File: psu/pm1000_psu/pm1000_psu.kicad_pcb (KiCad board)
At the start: 2 copper layers, 101.5 x 32 mm, 35 parts, among them J1 44V A, J2 44V B, J3 Screw_Terminal_01x04, J4 48V phantom, U1 LM317_TO-220, U2 LM317_TO-220, U3 LM317_TO-220

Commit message: rework the psu layout a bit
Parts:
- added C11: 100n, Capacitor_THT:C_Disc_D5.0mm_W2.5mm_P2.50mm, F.Cu at (96.0, 62.5)
- added C5: 100n, Capacitor_THT:C_Disc_D5.0mm_W2.5mm_P2.50mm, F.Cu at (52.2, 76.0)
- added C9: 100n, Capacitor_THT:C_Disc_D5.0mm_W2.5mm_P2.50mm, F.Cu at (115.8, 44.0)
- added D10: LED_Small, LED_THT:LED_D3.0mm, F.Cu at (88.0, 63.8)
- added D8: LED_Small, LED_THT:LED_D3.0mm, F.Cu at (116.5, 60.7)
- added D9: LED_Small, LED_THT:LED_D3.0mm, F.Cu at (47.0, 74.8)
- added J2: , Connector_Molex:Molex_KK-254_AE-6410-02A_1x02_P2.54mm_Vertical, F.Cu at (121.5, 54.7)
- added R12: 2k2, Resistor_THT:R_Axial_DIN0207_L6.3mm_D2.5mm_P10.16mm_Horizontal, F.Cu at (101.9, 57.0)
- added R13: 2k2, Resistor_THT:R_Axial_DIN0207_L6.3mm_D2.5mm_P10.16mm_Horizontal, F.Cu at (45.5, 56.6)
- added R14: 2k2, Resistor_THT:R_Axial_DIN0207_L6.3mm_D2.5mm_P10.16mm_Horizontal, F.Cu at (86.4, 58.5)
- added R3: 2k2, Resistor_THT:R_Axial_DIN0207_L6.3mm_D2.5mm_P10.16mm_Horizontal, F.Cu at (115.5, 58.1)
- J1: value 44V A -> (none)
- J3: value Screw_Terminal_01x04 -> (none)
- J4: value 48V phantom -> (none)
- J5: renamed from J2; value 44V B -> (none)
- R1, R2: footprint Resistor_THT:R_Axial_DIN0207_L6.3mm_D2.5mm_P10.16mm_Horizontal -> Resistor_THT:R_Axial_DIN0411_L9.9mm_D3.6mm_P15.24mm_Horizontal
- R6: renamed from R3; footprint Resistor_THT:R_Axial_DIN0207_L6.3mm_D2.5mm_P10.16mm_Horizontal -> Resistor_THT:R_Axial_DIN0411_L9.9mm_D3.6mm_P15.24mm_Horizontal
- R7: renamed from R4; footprint Resistor_THT:R_Axial_DIN0207_L6.3mm_D2.5mm_P10.16mm_Horizontal -> Resistor_THT:R_Axial_DIN0411_L9.9mm_D3.6mm_P15.24mm_Horizontal
- moved U3 13.2 mm to (80.5, 61.6)
- moved R8 12.0 mm to (112.6, 47.5), turned to 180 degrees
- moved RV1 4.21 mm to (54.0, 57.0)
- moved C8 4.08 mm to (115.3, 38.5)
- moved R10 3.43 mm to (102.4, 44.0)
- moved D6 3.39 mm to (101.9, 51.5)
- moved J4 2.99 mm to (121.5, 48.2)
- moved U1 2.98 mm to (67.0, 61.6)
- moved U2 2.98 mm to (109.0, 61.6)
- moved R2 2.98 mm to (56.9, 44.0)
- moved R1 2.95 mm to (56.9, 39.5)
- moved RV2 2.46 mm to (104.0, 39.0)
- moved R7 2.04 mm to (83.9, 44.0)
- moved R6 1.94 mm to (83.9, 39.5)
- moved D5 1.59 mm to (32.0, 56.5)
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- renumbered C7 to C10, C6 to C4, C4 to C6, C5 to C7, D3 to D2, D4 to D3, D5 to D4, D6 to D5, D7 to D6, D2 to D7, R8 to R11, R5 to R4, R7 to R5, R9 to R8, R6 to R9, RV3 to RV2, RV2 to RV3, U3 to U2, U2 to U3
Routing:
- net +44V B: track 54.4 -> 0.00 mm
- net unreg: track 123.9 -> 83.9 mm
- net Net-(C7-Pad1): track 35.5 -> 0.00 mm
- net Net-(C3-Pad1): track 34.6 -> 0.00 mm
- net +48V: track 30.9 -> 0.00 mm
- net +44V A: track 53.8 -> 27.4 mm
- net Net-(R10-Pad2): track 22.5 -> 0.00 mm
- net Net-(C2-Pad1): track 21.9 -> 0.00 mm
- net Net-(R11-Pad2): track 19.9 -> 0.00 mm
- net Net-(R4-Pad1): track 19.9 -> 0.00 mm
- net Net-(R11-Pad1): track 9.17 -> 0.00 mm
- net Net-(R5-Pad1): track 0.68 -> 6.75 mm
- net Net-(C6-Pad1): track 19.3 -> 22.3 mm
- net Net-(D3-Pad2): track 24.4 -> 21.9 mm
- net Net-(R10-Pad1): track 6.88 -> 5.68 mm
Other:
- board size 101.5 x 32 mm -> 105 x 35 mm

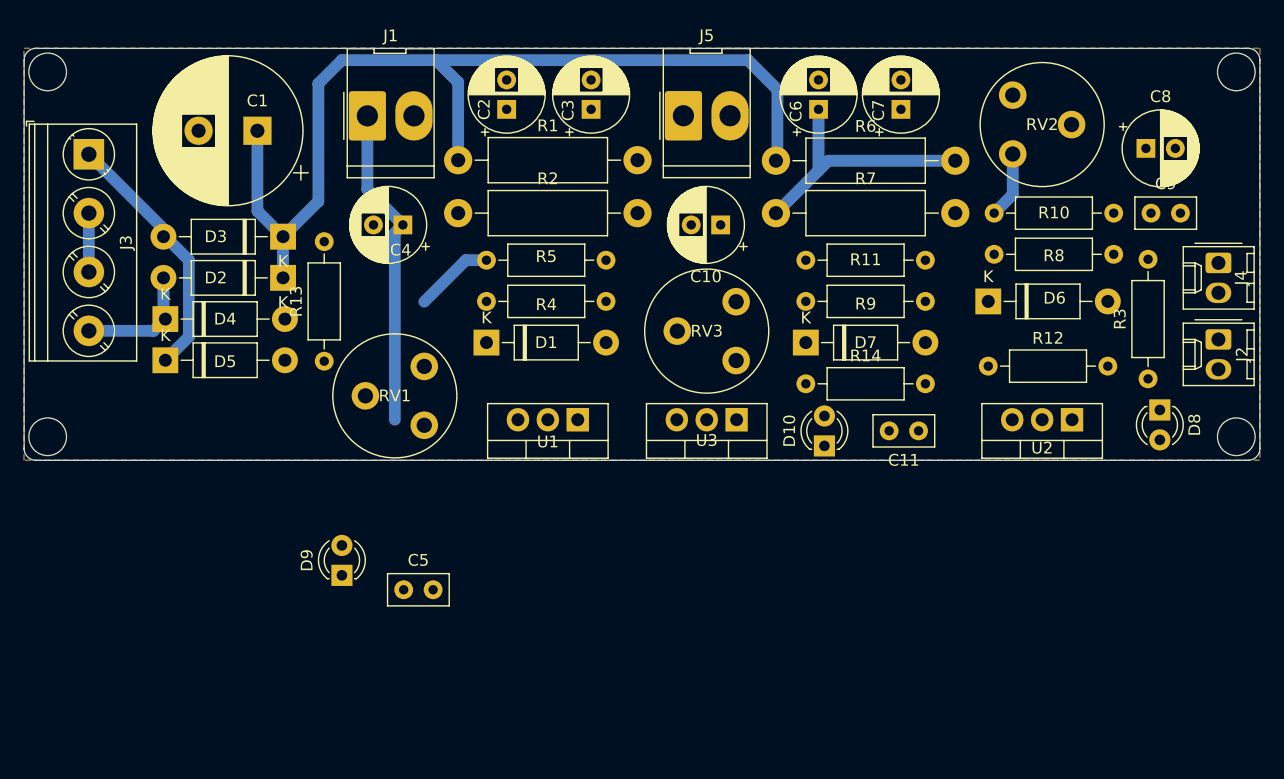
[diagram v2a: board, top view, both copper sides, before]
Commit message: simplify filter stages for 44v channels
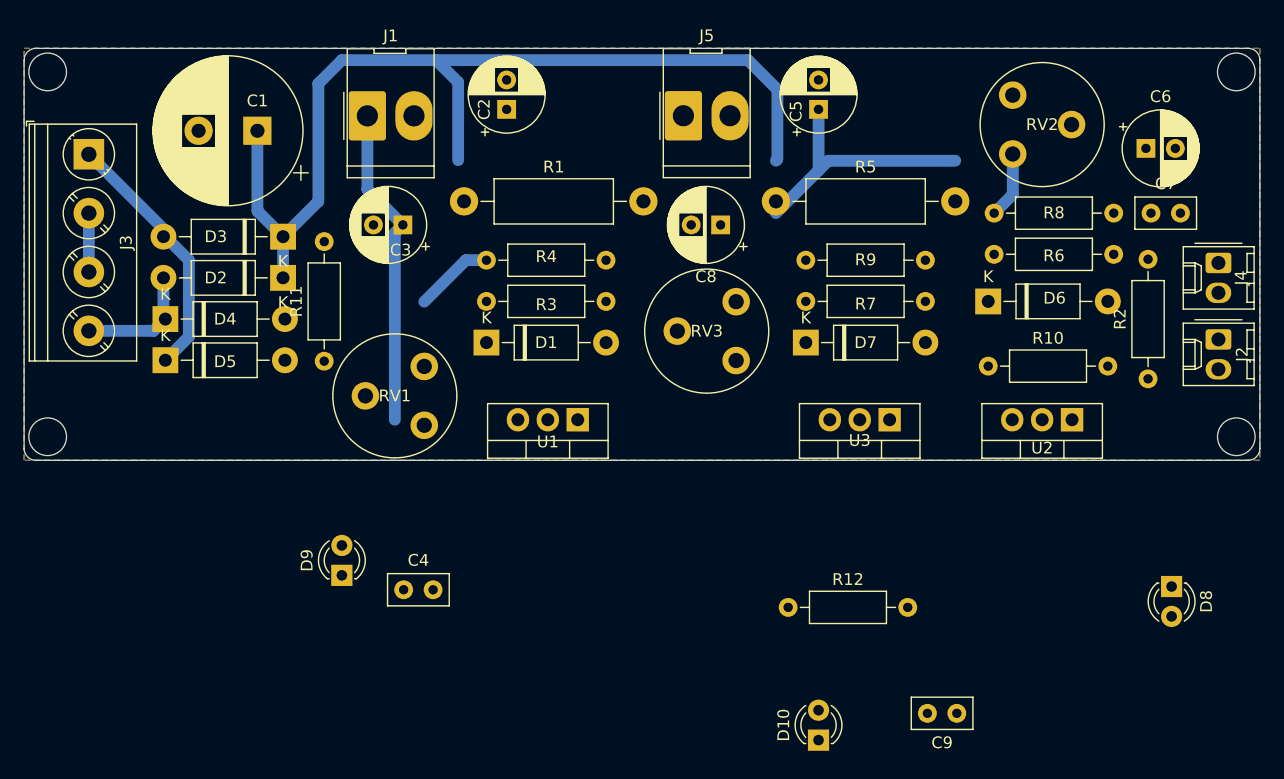
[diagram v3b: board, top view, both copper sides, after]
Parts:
- removed the C3 at (68.2, 35.2)
- removed the C7 at (94.5, 35.2)
- removed the R2 at (56.9, 44.0)
- removed the R7 at (83.9, 44.0)
- R1: value 1R 1W -> 10R 1W
- R5: renamed from R6; value 1R 1W -> 10R 1W
- moved D10 25.0 mm to (87.5, 88.8)
- moved C9 24.2 mm to (99.2, 86.5)
- moved R12 19.1 mm to (84.9, 77.5)
- moved D8 15.0 mm to (117.5, 75.7)
- moved U3 13.0 mm to (93.5, 61.6)
- moved R1 3.54 mm to (57.4, 43.0)
- moved R5 3.45 mm to (83.9, 43.0)
- renumbered C4 to C3, C5 to C4, C6 to C5, C8 to C6, C9 to C7, C10 to C8, C11 to C9, R12 to R10, R13 to R11, R14 to R12, R3 to R2, R4 to R3, R5 to R4, R8 to R6, R9 to R7, R10 to R8, R11 to R9
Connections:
- C5 pad 1: Net-(C6-Pad1) -> Net-(C5-Pad1)
- D1 pad 1: Net-(C3-Pad1) -> Net-(C2-Pad1)
- D7 pad 1: Net-(C7-Pad1) -> Net-(C5-Pad1)
- R5 pad 2: Net-(C6-Pad1) -> Net-(C5-Pad1)
- U1 pad 3: Net-(C3-Pad1) -> Net-(C2-Pad1)
- U3 pad 3: Net-(C7-Pad1) -> Net-(C5-Pad1)
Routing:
- net Net-(C6-Pad1): track 22.3 -> 0.00 mm
- net Net-(C5-Pad1): track 0.00 -> 22.3 mm

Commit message: new layout
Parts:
- R1, R5: value 10R 1W -> 100R 1W
- moved C9 48.3 mm to (76.8, 43.8)
- moved R12 34.0 mm to (80.7, 43.7), turned to -90 degrees
- moved D10 33.3 mm to (76.4, 57.4), turned to -90 degrees
- moved C4 32.1 mm to (50.0, 44.0), turned to 180 degrees
- moved J4 27.2 mm to (98.6, 33.5), turned to 0 degrees
- moved D8 23.4 mm to (102.8, 57.5)
- moved J2 21.7 mm to (116.4, 33.6), turned to 0 degrees
- moved C6 20.8 mm to (99.8, 52.4)
- moved RV1 19.4 mm to (61.0, 39.0), turned to 90 degrees
- moved C5 17.7 mm to (91.6, 52.4), turned to 0 degrees
- moved D9 17.6 mm to (49.8, 57.4), turned to -90 degrees
- moved C2 17.6 mm to (65.4, 52.2), turned to 0 degrees
- moved R11 15.4 mm to (54.1, 43.8), turned to -90 degrees
- moved C7 15.3 mm to (101.1, 39.4), turned to 180 degrees
- moved R5 14.7 mm to (93.4, 31.8), turned to -90 degrees
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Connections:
- R4 pad 1: Net-(R4-Pad1) -> GND
- R4 pad 2: Net-(R3-Pad1) -> Net-(RV1-Pad3)
- R8 pad 1: Net-(R8-Pad1) -> GND
- R8 pad 2: Net-(R6-Pad1) -> Net-(R8-Pad2)
- R9 pad 1: Net-(R9-Pad1) -> GND
- R9 pad 2: Net-(R7-Pad1) -> Net-(R9-Pad2)
- RV1 pad 1: Net-(R4-Pad1) -> Net-(R3-Pad1)
- RV1 pad 2: GND -> Net-(R3-Pad1)
- RV1 pad 3: GND -> Net-(RV1-Pad3)
- RV2 pad 1: Net-(R8-Pad1) -> Net-(R6-Pad1)
- RV2 pad 2: GND -> Net-(R6-Pad1)
- RV2 pad 3: GND -> Net-(R8-Pad2)
- RV3 pad 1: Net-(R9-Pad1) -> Net-(R7-Pad1)
- RV3 pad 2: GND -> Net-(R7-Pad1)
- RV3 pad 3: GND -> Net-(R9-Pad2)
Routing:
- net unreg: track 83.9 -> 0.00 mm
- net +44V A: track 27.4 -> 0.00 mm
- net Net-(C5-Pad1): track 22.3 -> 0.00 mm
- net Net-(D3-Pad2): track 21.9 -> 0.66 mm
- net Net-(D2-Pad2): track 10.5 -> 0.00 mm
- net Net-(R4-Pad1): track 6.75 -> 0.00 mm
- net Net-(R8-Pad1): track 5.68 -> 0.00 mm
- net Net-(J3-Pad2): track 5.00 -> 0.00 mm

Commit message: route psu pcb
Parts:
- moved C6 2.45 mm to (102.2, 52.4), turned to 180 degrees
- moved RV3 0.25 mm to (87.7, 39.0)
- moved R5 0.15 mm to (93.2, 31.8)
- moved RV1 0.07 mm to (61.0, 39.0)
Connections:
- J1 pad 1: +44V A -> GND
- J1 pad 2: GND -> +44V A
- J2 pad 1: Net-(J2-Pad1) -> GND
- J2 pad 2: GND -> Net-(J2-Pad2)
- J4 pad 1: +48V -> GND
- J4 pad 2: GND -> +48V
- J5 pad 1: +44V B -> GND
- J5 pad 2: GND -> +44V B
- R2 pad 1: Net-(J2-Pad1) -> Net-(J2-Pad2)
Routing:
- net unreg: track 0.00 -> 119.2 mm
- net +48V: track 0.00 -> 57.2 mm
- net +44V B: track 0.00 -> 47.0 mm
- net +44V A: track 0.00 -> 46.8 mm
- net Net-(R6-Pad1): track 0.00 -> 34.1 mm
- net Net-(R7-Pad1): track 0.00 -> 30.0 mm
- net Net-(R3-Pad1): track 0.00 -> 29.9 mm
- net Net-(D3-Pad2): track 0.66 -> 30.2 mm
- net Net-(C2-Pad1): track 0.00 -> 26.6 mm
- net Net-(C5-Pad1): track 0.00 -> 26.3 mm
- net Net-(J2-Pad2): track 0.00 -> 11.2 mm
- net Net-(D2-Pad2): track 0.00 -> 10.6 mm
- net Net-(R8-Pad2): track 0.00 -> 6.24 mm
- net Net-(D10-Pad1): track 0.00 -> 5.76 mm
- net Net-(D9-Pad1): track 0.00 -> 5.71 mm
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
